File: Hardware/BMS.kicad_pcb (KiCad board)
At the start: 4 copper layers, 109 x 148 mm, 365 parts, among them IC1 STM32H742VIT6, IC2 TPS563200DDCR, J1 Conn_01x28, J10 Conn_01x10, J11 USB4235-03-C_REVA, J13 USB_A, J16 Conn_01x10, J19 Conn_02x13_Counter_Clockwise, J7 FTSH-107-01-L-D-K, Q2 100V/2W, Q5 DMT6018LDR-7, Q7 DMT6018LDR-7, Q8 100V/2W, SW1 SW_Push, U1 BQ79614PAPRQ1, U2 BQ79614PAPRQ1, U3 PBQ79600PWQ1, U4 MCP2542FD-E/MF, U5 PTPSM863253RDXR

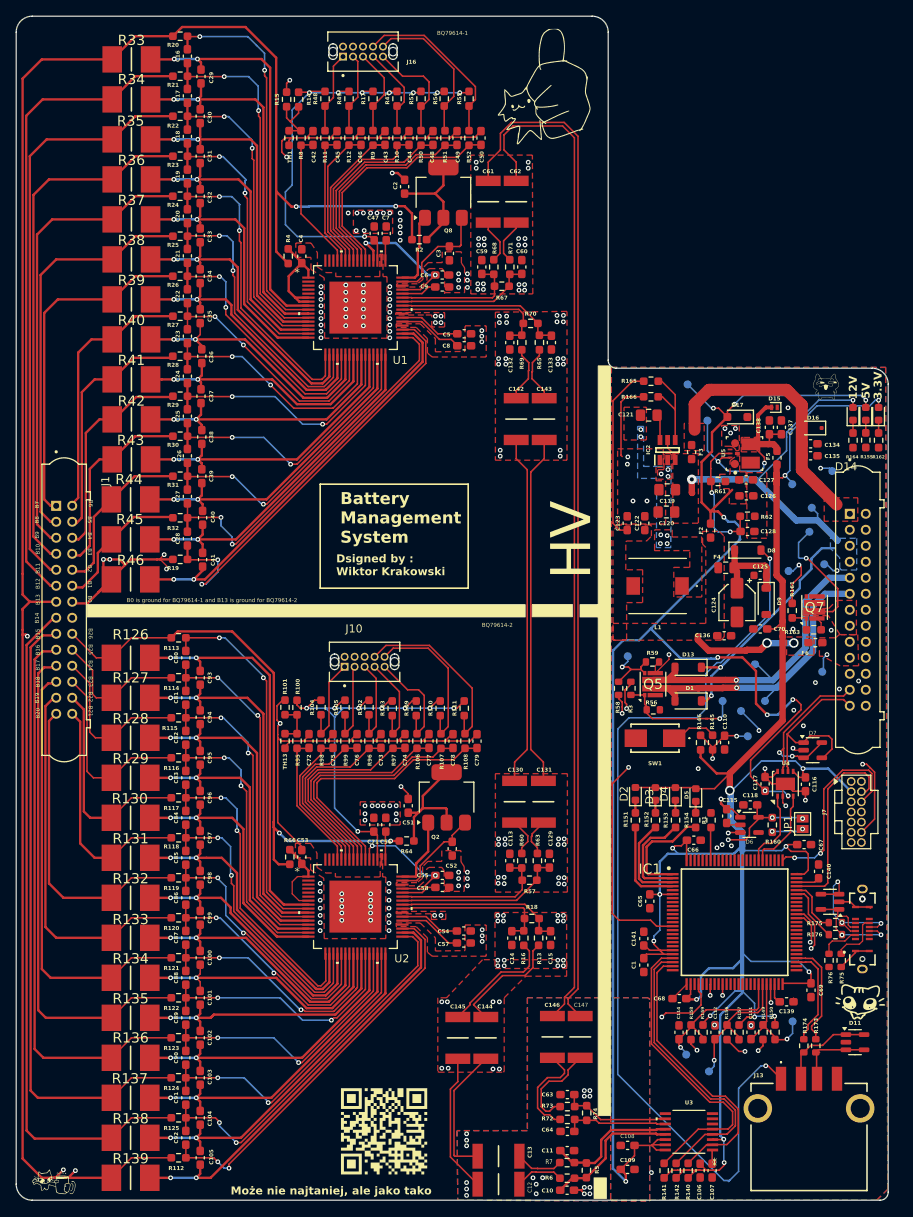
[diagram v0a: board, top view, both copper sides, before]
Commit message: poprawiono impedancje na lini usb na 89ohm ( w zakresie)
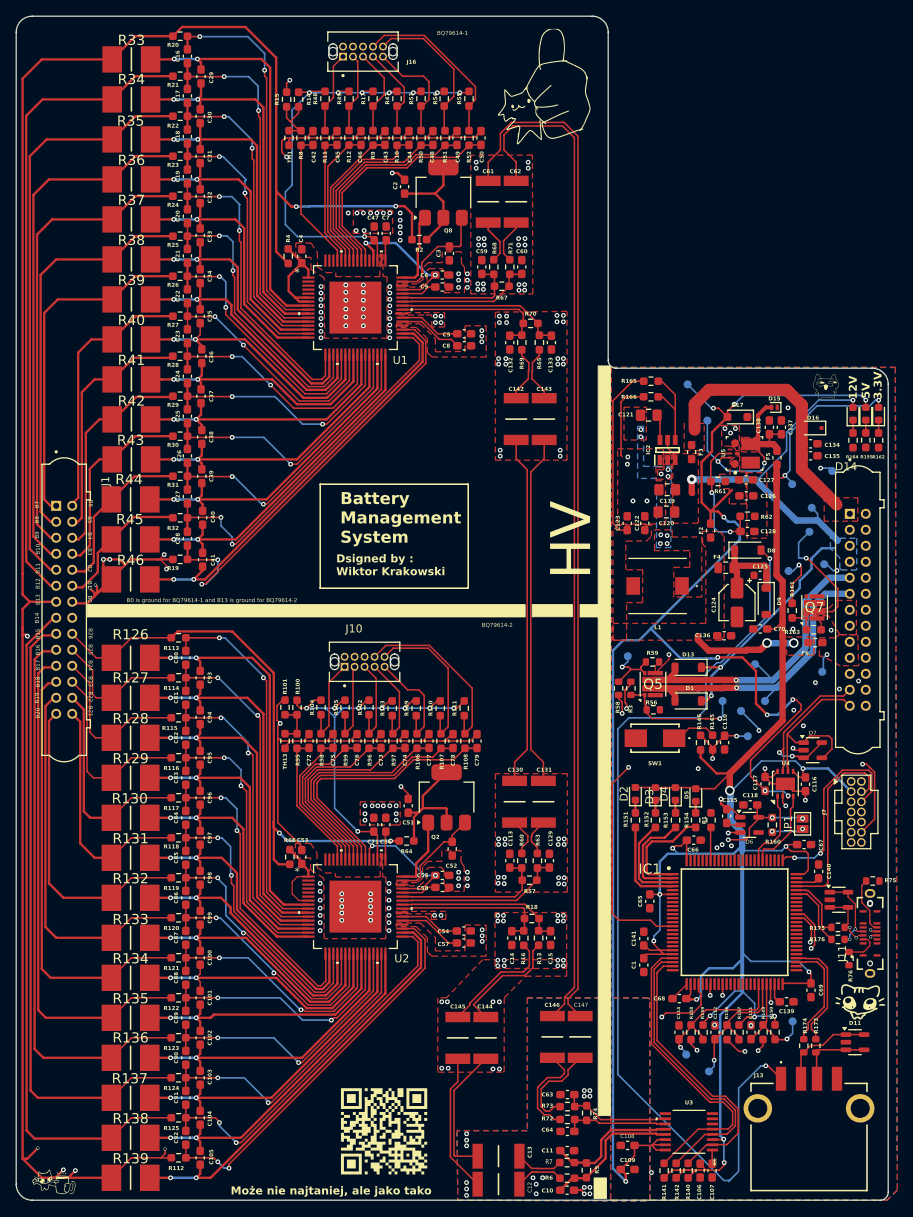
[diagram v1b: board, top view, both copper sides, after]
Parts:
- moved R75 10.7 mm to (185.0, 145.0), turned to 180 degrees
- moved R76 2.51 mm to (182.0, 154.7)
- moved D12 1.14 mm to (180.7, 147.3), turned to 0 degrees
- moved J11 1.11 mm to (184.6, 151.6)
- moved R175 0.68 mm to (180.6, 150.8)
- moved R176 0.68 mm to (180.6, 152.3)
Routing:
- net GND: track 48.9 -> 40.1 mm
- net /Connectivity/USB1_DP: track 18.3 -> 11.4 mm
- net Batt_Coupling: track 305.9 -> 309.7 mm, vias 92 -> 94
- net Stack-: track 65.8 -> 68.2 mm, vias 100 -> 102
- net /Connectivity/USB1_DN: track 16.0 -> 14.1 mm, vias 2 -> 3
- net /USB-: track 7.33 -> 8.90 mm
- net /USB2-: track 12.7 -> 13.7 mm
- net /USB+: track 6.89 -> 7.86 mm
- net /USB2+: track 13.5 -> 14.4 mm
- net Net-(J11-CC1): track 4.99 -> 4.38 mm

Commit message: poprawiono impedancje na sciezkach sygnalowych miedzy ukladami bq
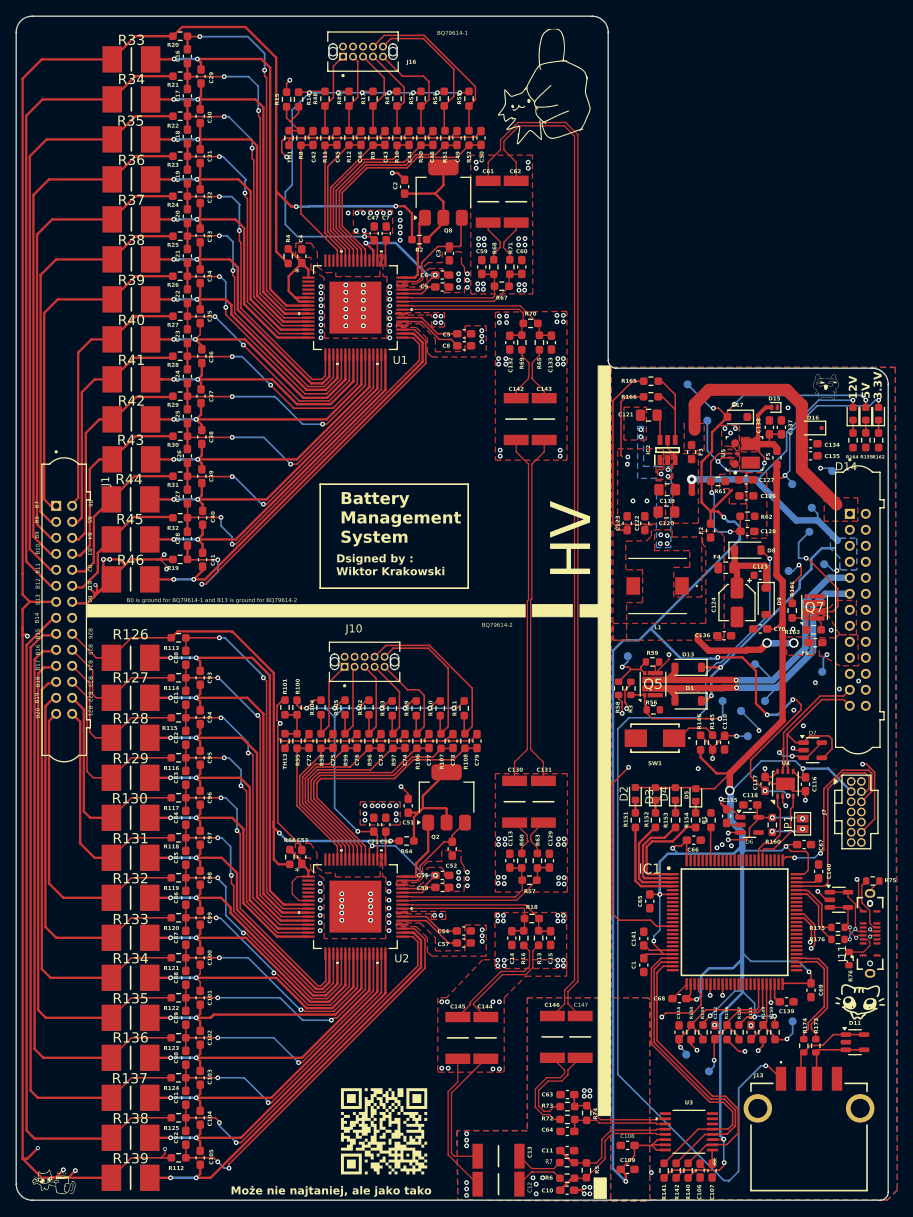
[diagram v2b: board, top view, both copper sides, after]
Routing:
- net GND: track 40.1 -> 48.4 mm, vias 41 -> 43

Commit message: Wersja V1.0 gotowa, wysłana do produckji
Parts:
- removed D15: TVS diode 3.3V, Diode_SMD:D_SOD-882
- added REF**: MountingHole_2.2mm_M2_Pad_Via, MountingHole:MountingHole_2.2mm_M2_Pad_Via, F.Cu at (148.9, 40.0)
- added REF**: MountingHole_2.2mm_M2_Pad_Via, MountingHole:MountingHole_2.2mm_M2_Pad_Via, F.Cu at (183.9, 160.7)
- added REF**: MountingHole_2.2mm_M2_Pad_Via, MountingHole:MountingHole_2.2mm_M2_Pad_Via, F.Cu at (81.0, 40.0)
- added REF**: MountingHole_2.2mm_M2_Pad_Via, MountingHole:MountingHole_2.2mm_M2_Pad_Via, F.Cu at (81.2, 181.6)
- added REF**: MountingHole_2.2mm_M2_Pad_Via, MountingHole:MountingHole_2.2mm_M2_Pad_Via, F.Cu at (130.0, 182.2)
- moved G*** 28.3 mm to (156.8, 169.9)
- moved G*** 27.3 mm to (117.4, 174.7)
- moved G*** 8.04 mm to (83.2, 174.2)
- moved G*** 3.73 mm to (120.2, 176.2)
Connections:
- U2 pad 52: unconnected-(U2-RX-Pad52) -> /Mesurements_LTC2/to_rx
- U2 pad 53: /Mesurements_LTC2/to_rx -> unconnected-(U2-TX-Pad53)
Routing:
- net Batt_Coupling: track 309.7 -> 303.8 mm
- net VBUS: track 117.9 -> 118.5 mm
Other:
- board text added: "Battery Management System V1.0"
- board text removed: "Battery Management System"
